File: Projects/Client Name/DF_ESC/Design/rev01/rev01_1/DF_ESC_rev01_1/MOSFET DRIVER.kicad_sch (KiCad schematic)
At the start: 0 parts

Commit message: Update 19-01-2024 primera
cambiar y añadir numeracion de sheets
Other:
- note added: "[5] - MOSFET DRIVER"
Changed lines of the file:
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@@
     (comment 4 "Ivan Mendez")
   )
+  (text "[5] - MOSFET DRIVER" (at 85.09 27.94 0)
+    (effects (font (size 8 8) bold) (justify left bottom))
+  )
 )

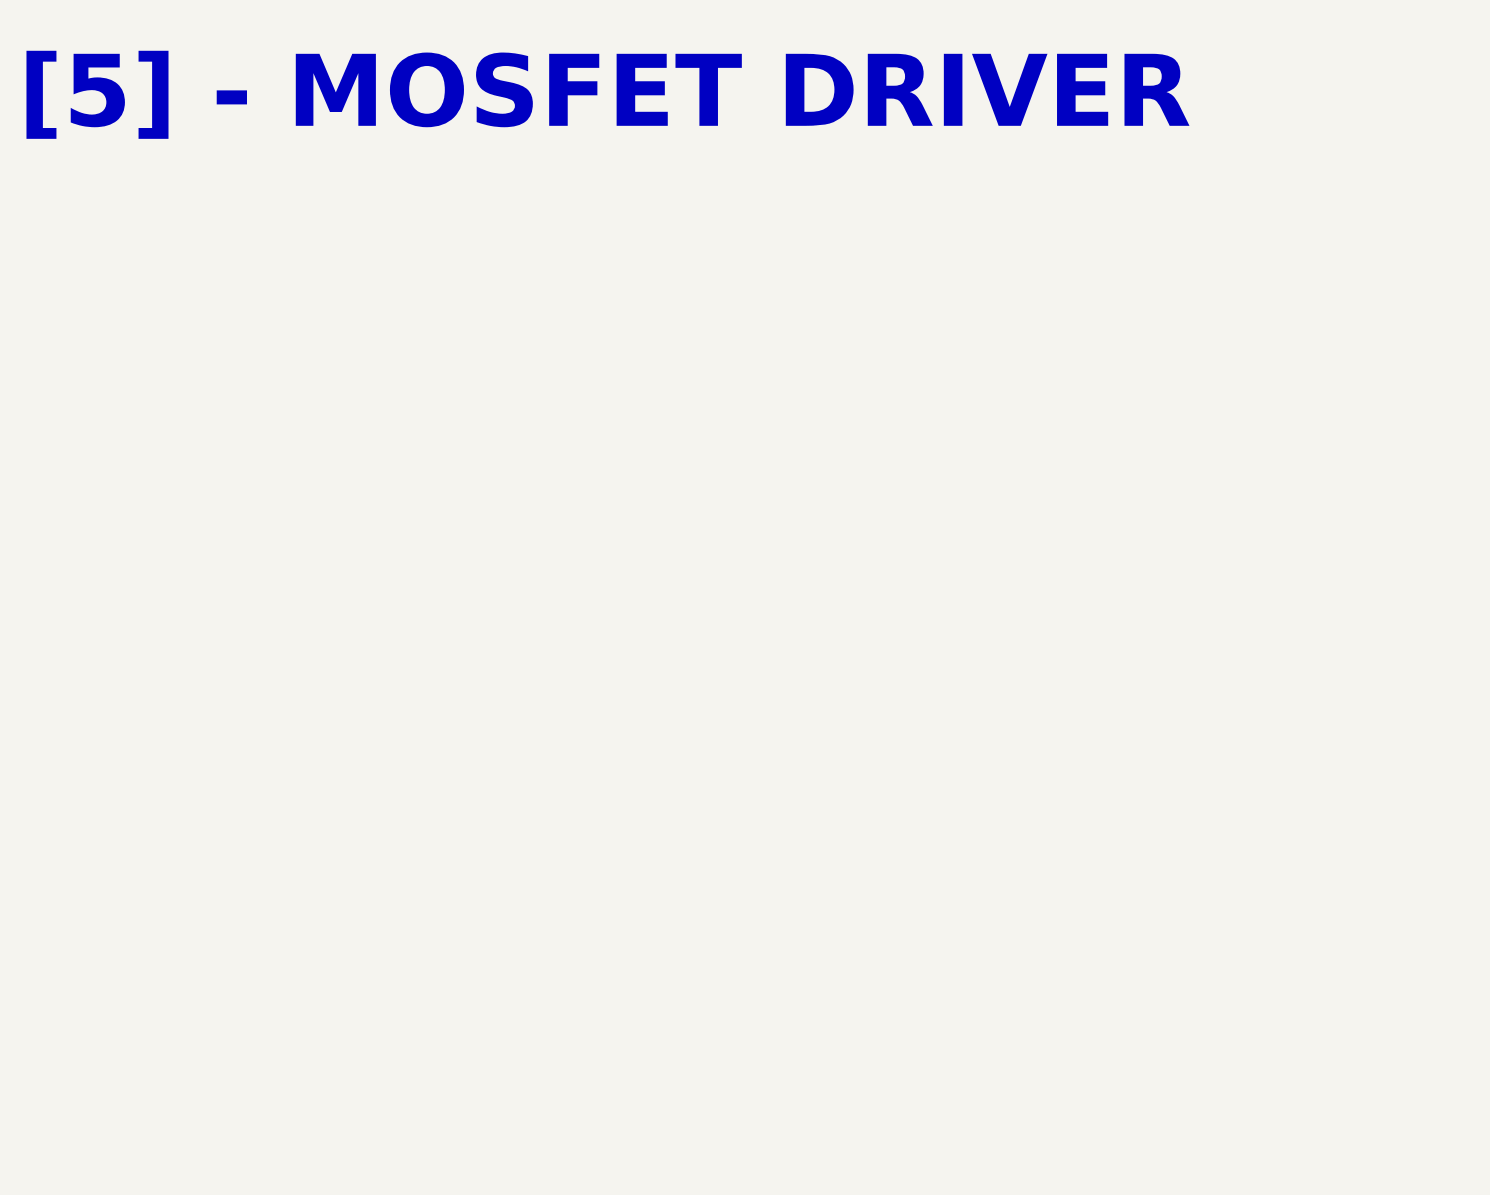
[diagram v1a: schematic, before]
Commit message: Update 22-01-2023_1
DRV8302 Symbol
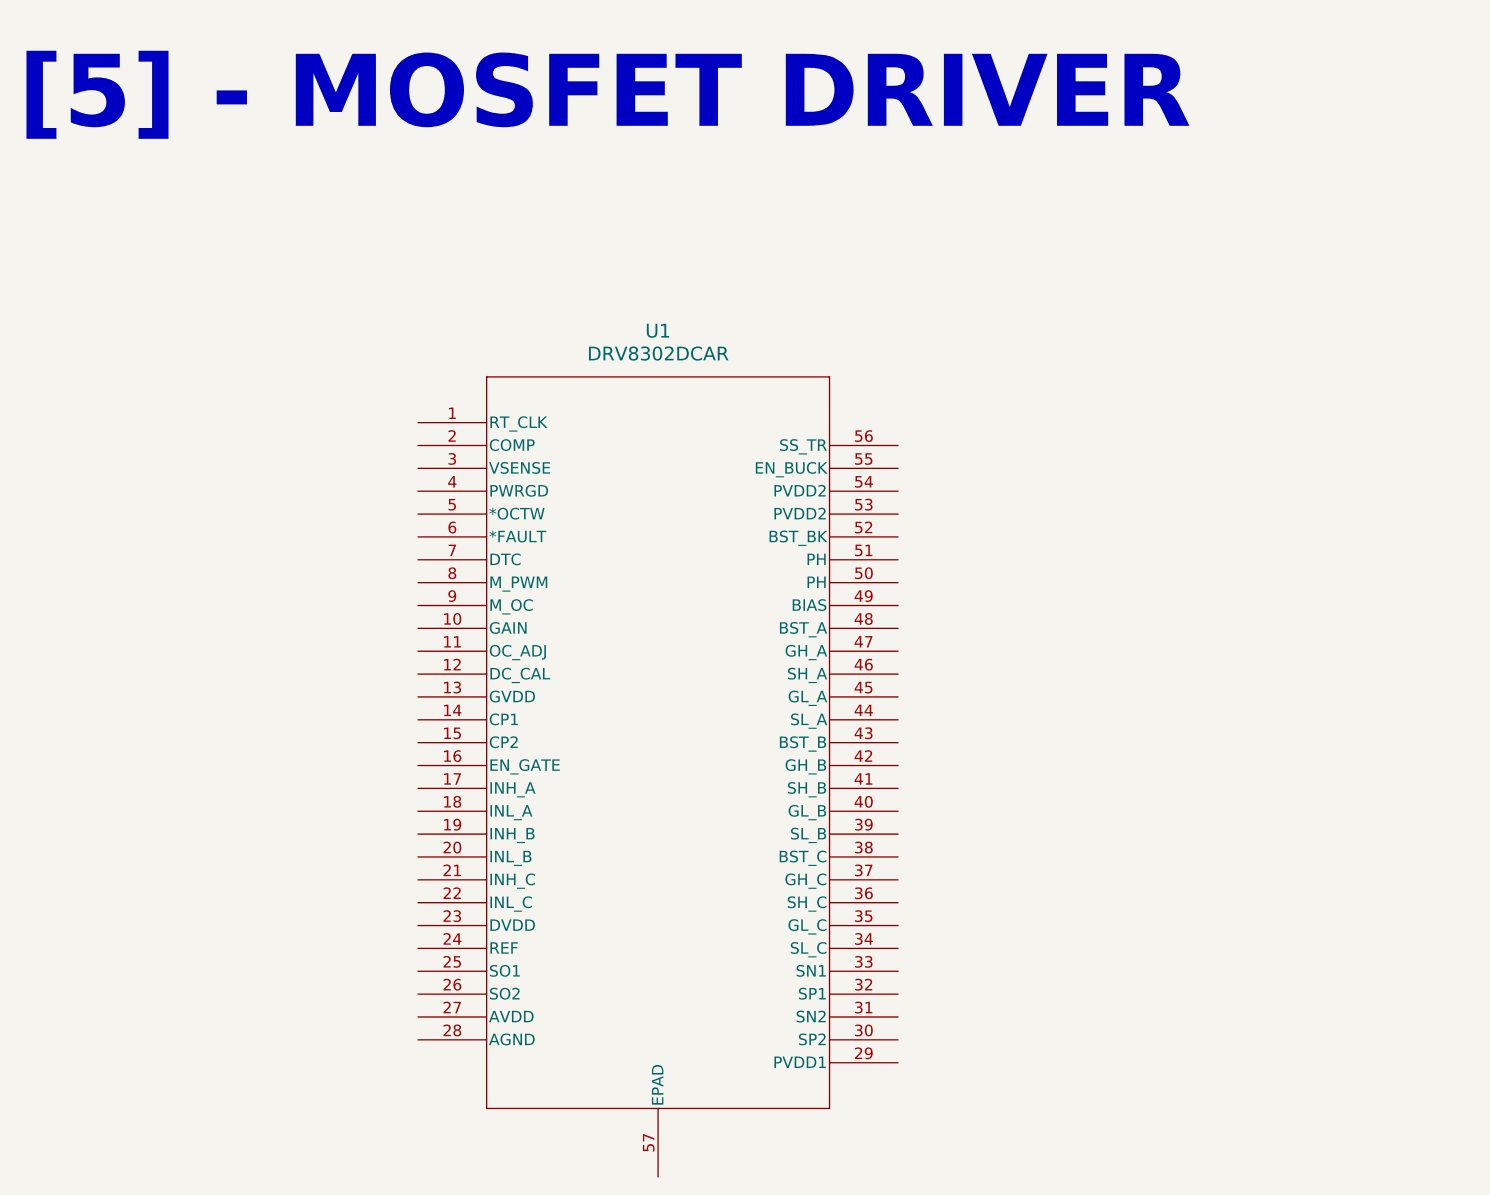
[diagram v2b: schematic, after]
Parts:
- added U1: DRV8302DCAR, DCA56_6P35X3P61, symbol DRV8302:DRV8302DCAR
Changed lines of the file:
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@@
     (effects (font (size 8 8) bold) (justify left bottom))
   )
+  (symbol (lib_id "DRV8302:DRV8302DCAR") (at 129.54 59.69 0) (unit 1)
+    (in_bom yes) (on_board yes) (dnp no) (fields_autoplaced)
+    (property "Reference" "U1" (at 156.21 49.53 0)
+      (effects (font (size 1.524 1.524)))
+    )
+    (property "Value" "DRV8302DCAR" (at 156.21 52.07 0)
+      (effects (font (size 1.524 1.524)))
+    )
+    (property "Footprint" "DCA56_6P35X3P61" (at 157.48 53.34 0)
+      (effects (font (size 1.27 1.27) italic) hide)
+    )
+    (property "Datasheet" "DRV8302DCAR" (at 157.48 50.8 0)
+      (effects (font (size 1.27 1.27) italic) hide)
+    )
+    (pin "42")
+    (pin "12")
+    (pin "56")
+    (pin "14")
+    (pin "54")
+    (pin "34")
+    (pin "27")
+    (pin "36")
+    (pin "39")
+    (pin "28")
+    (pin "37")
+    (pin "55")
+    (pin "3")
+    (pin "7")
+    (pin "19")
+    (pin "38")
+    (pin "24")
+    (pin "43")
+    (pin "45")
+    (pin "5")
+    (pin "17")
+    (pin "2")
+    (pin "21")
+    (pin "47")
+    (pin "40")
+    (pin "30")
+    (pin "50")
+    (pin "51")
+    (pin "9")
+    (pin "23")
+    (pin "10")
+    (pin "13")
+    (pin "26")
+    (pin "35")
+    (pin "29")
+    (pin "33")
+    (pin "48")
+    (pin "49")
+    (pin "16")
+    (pin "1")
+    (pin "25")
+    (pin "41")
+    (pin "11")
+    (pin "52")
+    (pin "57")
+    (pin "53")
+    (pin "15")
+    (pin "44")
+    (pin "46")
+    (pin "4")
+    (pin "31")
+    (pin "22")
+    (pin "6")
+    (pin "8")
+    (pin "20")
+    (pin "32")
+    (pin "18")
+    (instances
+      (project "DF_ESC_rev01_1"
+        (path "/e63e39d7-6ac0-4ffd-8aa3-1841a4541b55/ebfeafe7-4d70-4ef9-bb18-a00f088a6e19"
+          (reference "U1") (unit 1)
+        )
+      )
+    )
+  )
 )

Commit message: Udpate 23-01-2024_Prueba
Solo se borro para probar cambio de carpeta KICAD_directorio por Github
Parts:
- removed U1: DRV8302DCAR, DCA56_6P35X3P61, symbol DRV8302:DRV8302DCAR
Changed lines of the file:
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@@
     (effects (font (size 8 8) bold) (justify left bottom))
   )
-  (symbol (lib_id "DRV8302:DRV8302DCAR") (at 129.54 59.69 0) (unit 1)
-    (in_bom yes) (on_board yes) (dnp no) (fields_autoplaced)
-    (property "Reference" "U1" (at 156.21 49.53 0)
-      (effects (font (size 1.524 1.524)))
-    )
-    (property "Value" "DRV8302DCAR" (at 156.21 52.07 0)
-      (effects (font (size 1.524 1.524)))
-    )
-    (property "Footprint" "DCA56_6P35X3P61" (at 157.48 53.34 0)
-      (effects (font (size 1.27 1.27) italic) hide)
-    )
-    (property "Datasheet" "DRV8302DCAR" (at 157.48 50.8 0)
-      (effects (font (size 1.27 1.27) italic) hide)
-    )
-    (pin "42")
-    (pin "12")
-    (pin "56")
-    (pin "14")
-    (pin "54")
-    (pin "34")
-    (pin "27")
-    (pin "36")
-    (pin "39")
-    (pin "28")
-    (pin "37")
-    (pin "55")
-    (pin "3")
-    (pin "7")
-    (pin "19")
-    (pin "38")
-    (pin "24")
-    (pin "43")
-    (pin "45")
-    (pin "5")
-    (pin "17")
-    (pin "2")
-    (pin "21")
-    (pin "47")
-    (pin "40")
-    (pin "30")
-    (pin "50")
-    (pin "51")
-    (pin "9")
-    (pin "23")
-    (pin "10")
-    (pin "13")
-    (pin "26")
-    (pin "35")
-    (pin "29")
-    (pin "33")
-    (pin "48")
-    (pin "49")
-    (pin "16")
-    (pin "1")
-    (pin "25")
-    (pin "41")
-    (pin "11")
-    (pin "52")
-    (pin "57")
-    (pin "53")
-    (pin "15")
-    (pin "44")
-    (pin "46")
-    (pin "4")
-    (pin "31")
-    (pin "22")
-    (pin "6")
-    (pin "8")
-    (pin "20")
-    (pin "32")
-    (pin "18")
-    (instances
-      (project "DF_ESC_rev01_1"
-        (path "/e63e39d7-6ac0-4ffd-8aa3-1841a4541b55/ebfeafe7-4d70-4ef9-bb18-a00f088a6e19"
-          (reference "U1") (unit 1)
-        )
-      )
-    )
-  )
 )
